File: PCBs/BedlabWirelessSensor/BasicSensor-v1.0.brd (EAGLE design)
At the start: 41.6 x 50.2 mm, 18 parts, among them U1 ATMEGA328P_PDIP

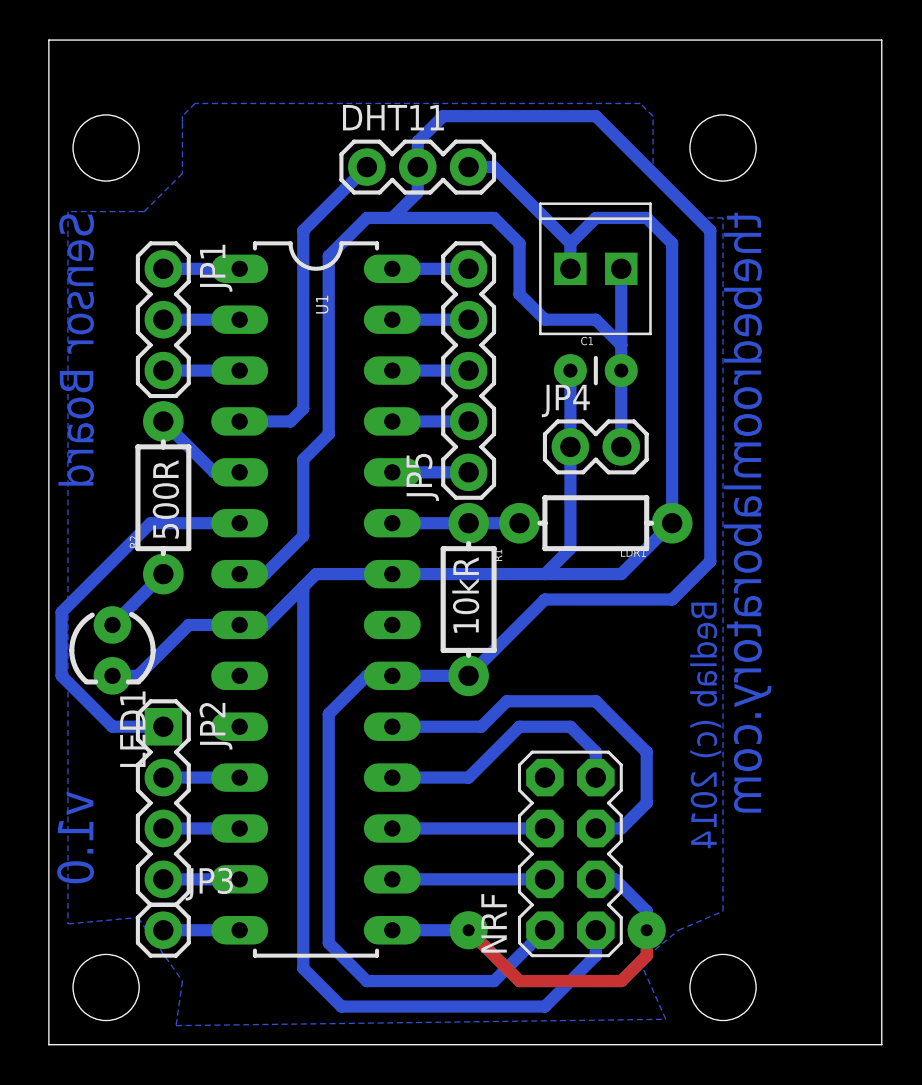
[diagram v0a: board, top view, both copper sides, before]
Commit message: Tiled PCB layout added for printing tomorrow. Additionally, changes made to arduino sketches to add funtionality for LDR, LED, Temp/humid sensor and switching the lights on/off from the gateway.
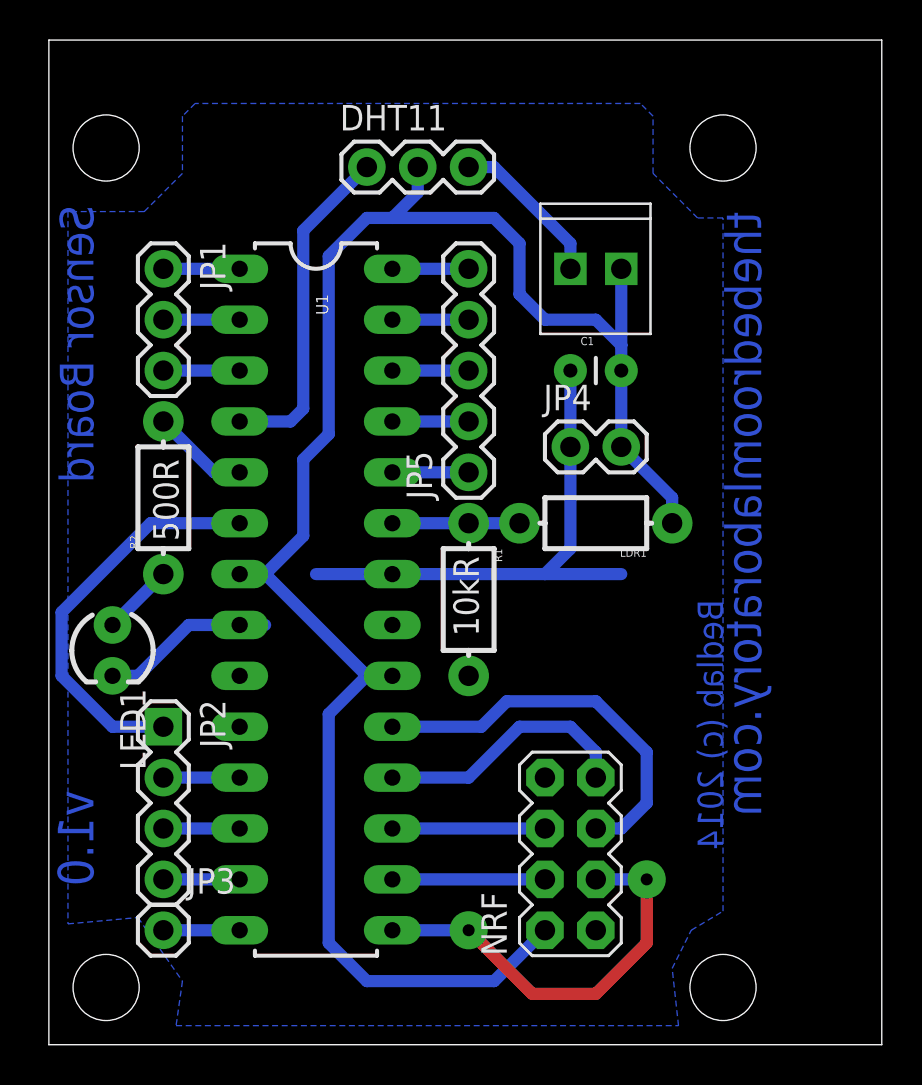
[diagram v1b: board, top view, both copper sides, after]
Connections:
- net GND: now also R1.P$2; no longer LDR1.P$1
- net VCC: now also LDR1.P$1; no longer R1.P$2
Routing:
- net GND: track 106.6 -> 42.5 mm
- net VCC: track 131.5 -> 90.0 mm
- net N$5: track 19.7 -> 20.8 mm
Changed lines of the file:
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@@
 <wire x1="0" y1="50.155" x2="0" y2="0" width="0" layer="20"/>
 <text x="35.56" y="41.5925" size="1.778" layer="16" rot="SMR270">thebedroomlaboratory.com</text>
-<text x="33.3375" y="22.225" size="1.27" layer="16" rot="SMR270">Bedlab (c) 2014</text>
-<text x="2.2225" y="41.5925" size="1.6764" layer="16" rot="SMR270">Sensor Board</text>
+<text x="33.655" y="22.225" size="1.27" layer="16" rot="SMR270">Bedlab (c) 2014</text>
+<text x="2.2225" y="41.91" size="1.6764" layer="16" rot="SMR270">Sensor Board</text>
 <text x="2.2225" y="12.7" size="1.778" layer="16" rot="SMR270">v1.0</text>
 <dimension x1="0" y1="50.155" x2="36.195" y2="47.625" x3="18.0975" y3="47.625" textsize="1.778" layer="16" dtype="horizontal"/>
@@
 </signal>
 <signal name="VCC">
-<contactref element="R1" pad="P$2"/>
 <contactref element="DHT11" pad="2"/>
 <contactref element="U1" pad="20"/>
@@
 <wire x1="13.97" y1="5.08" x2="13.97" y2="16.51" width="0.6096" layer="16"/>
 <wire x1="13.97" y1="16.51" x2="15.875" y2="18.415" width="0.6096" layer="16"/>
-<wire x1="15.875" y1="18.415" x2="17.145" y2="18.415" width="0.6096" layer="16"/>
 <wire x1="28.575" y1="33.655" x2="28.575" y2="34.925" width="0.6096" layer="16"/>
 <wire x1="28.575" y1="38.735" x2="28.575" y2="34.925" width="0.6096" layer="16"/>
@@
 <wire x1="12.7" y1="29.21" x2="13.97" y2="30.48" width="0.6096" layer="16"/>
 <wire x1="13.97" y1="30.48" x2="13.97" y2="39.37" width="0.6096" layer="16"/>
-<wire x1="20.955" y1="18.415" x2="24.765" y2="22.225" width="0.6096" layer="16"/>
-<wire x1="24.765" y1="22.225" x2="31.115" y2="22.225" width="0.6096" layer="16"/>
-<wire x1="31.115" y1="22.225" x2="33.02" y2="24.13" width="0.6096" layer="16"/>
-<wire x1="33.02" y1="24.13" x2="33.02" y2="40.64" width="0.6096" layer="16"/>
-<wire x1="33.02" y1="40.64" x2="27.305" y2="46.355" width="0.6096" layer="16"/>
-<wire x1="27.305" y1="46.355" x2="19.685" y2="46.355" width="0.6096" layer="16"/>
-<wire x1="19.685" y1="46.355" x2="18.415" y2="45.085" width="0.6096" layer="16"/>
-<wire x1="18.415" y1="45.085" x2="18.415" y2="43.815" width="0.6096" layer="16"/>
-<wire x1="17.145" y1="18.415" x2="20.955" y2="18.415" width="0.6096" layer="16"/>
+<contactref element="LDR1" pad="P$1"/>
+<wire x1="28.575" y1="29.845" x2="31.115" y2="27.305" width="0.6096" layer="16"/>
+<wire x1="31.115" y1="27.305" x2="31.115" y2="26.035" width="0.6096" layer="16"/>
+<wire x1="10.795" y1="23.495" x2="15.875" y2="18.415" width="0.6096" layer="16"/>
+<wire x1="15.875" y1="18.415" x2="17.145" y2="18.415" width="0.6096" layer="16"/>
 </signal>
 <signal name="GND">
-<contactref element="LDR1" pad="P$1"/>
 <contactref element="DHT11" pad="3"/>
 <contactref element="U1" pad="8"/>
@@
 <contactref element="C1" pad="1"/>
 <contactref element="JP4" pad="1"/>
-<wire x1="24.765" y1="1.905" x2="14.605" y2="1.905" width="0.6096" layer="16"/>
 <wire x1="3.175" y1="18.415" x2="4.445" y2="18.415" width="0.6096" layer="16"/>
 <wire x1="4.445" y1="18.415" x2="6.985" y2="20.955" width="0.6096" layer="16"/>
@@
 <wire x1="26.035" y1="24.765" x2="24.765" y2="23.495" width="0.6096" layer="16"/>
 <wire x1="24.765" y1="23.495" x2="17.145" y2="23.495" width="0.6096" layer="16"/>
-<wire x1="31.115" y1="26.035" x2="28.575" y2="23.495" width="0.6096" layer="16"/>
 <wire x1="28.575" y1="23.495" x2="24.765" y2="23.495" width="0.6096" layer="16"/>
 <wire x1="26.035" y1="38.735" x2="26.035" y2="40.005" width="0.6096" layer="16"/>
-<wire x1="26.035" y1="40.005" x2="27.305" y2="41.275" width="0.6096" layer="16"/>
-<wire x1="27.305" y1="41.275" x2="29.845" y2="41.275" width="0.6096" layer="16"/>
-<wire x1="29.845" y1="41.275" x2="31.115" y2="40.005" width="0.6096" layer="16"/>
-<wire x1="31.115" y1="40.005" x2="31.115" y2="26.035" width="0.6096" layer="16"/>
 <wire x1="26.035" y1="40.005" x2="22.225" y2="43.815" width="0.6096" layer="16"/>
 <wire x1="22.225" y1="43.815" x2="20.955" y2="43.815" width="0.6096" layer="16"/>
-<wire x1="14.605" y1="1.905" x2="12.7" y2="3.81" width="0.6096" layer="16"/>
-<wire x1="12.7" y1="3.81" x2="12.7" y2="22.86" width="0.6096" layer="16"/>
-<wire x1="12.7" y1="22.86" x2="10.795" y2="20.955" width="0.6096" layer="16"/>
 <wire x1="10.795" y1="20.955" x2="9.525" y2="20.955" width="0.6096" layer="16"/>
 <wire x1="17.145" y1="23.495" x2="13.335" y2="23.495" width="0.6096" layer="16"/>
-<wire x1="13.335" y1="23.495" x2="12.7" y2="22.86" width="0.6096" layer="16"/>
-<wire x1="27.305" y1="5.715" x2="27.305" y2="4.445" width="0.6096" layer="16"/>
-<wire x1="27.305" y1="4.445" x2="24.765" y2="1.905" width="0.6096" layer="16"/>
 <polygon width="0.4064" layer="16">
-<vertex x="6.6675" y="46.0375"/>
+<vertex x="6.6675" y="46.355"/>
 <vertex x="6.6675" y="43.4975"/>
 <vertex x="4.7625" y="41.5925"/>
@@
 <vertex x="6.6675" y="3.175"/>
 <vertex x="6.35" y="0.9525"/>
-<vertex x="30.7975" y="1.27"/>
-<vertex x="29.5275" y="4.1275"/>
-<vertex x="31.4325" y="5.715"/>
+<vertex x="31.4325" y="0.9525"/>
+<vertex x="31.115" y="3.81"/>
+<vertex x="32.0675" y="5.715"/>
 <vertex x="33.655" y="6.6675"/>
 <vertex x="33.655" y="41.275"/>
@@
 <vertex x="29.5275" y="46.99"/>
 <vertex x="7.3025" y="46.99"/>
-<vertex x="6.6675" y="46.355"/>
 </polygon>
+<contactref element="R1" pad="P$2"/>
 </signal>
 <signal name="N$2">
@@
 <wire x1="17.145" y1="5.715" x2="20.955" y2="5.715" width="0.6096" layer="16"/>
 <via x="20.955" y="5.715" extent="1-16" drill="0.6" diameter="1.905"/>
-<via x="29.845" y="5.715" extent="1-16" drill="0.6" diameter="1.905"/>
-<wire x1="20.955" y1="5.715" x2="23.495" y2="3.175" width="0.6096" layer="1"/>
-<wire x1="23.495" y1="3.175" x2="28.575" y2="3.175" width="0.6096" layer="1"/>
-<wire x1="28.575" y1="3.175" x2="29.845" y2="4.445" width="0.6096" layer="1"/>
-<wire x1="29.845" y1="4.445" x2="29.845" y2="5.715" width="0.6096" layer="1"/>
-<wire x1="27.305" y1="8.255" x2="28.2575" y2="8.255" width="0.6096" layer="16"/>
-<wire x1="28.2575" y1="8.255" x2="29.845" y2="6.6675" width="0.6096" layer="16"/>
-<wire x1="29.845" y1="6.6675" x2="29.845" y2="5.715" width="0.6096" layer="16"/>
+<via x="29.845" y="8.255" extent="1-16" drill="0.6" diameter="1.905"/>
+<wire x1="20.955" y1="5.715" x2="24.13" y2="2.54" width="0.6096" layer="1"/>
+<wire x1="24.13" y1="2.54" x2="27.305" y2="2.54" width="0.6096" layer="1"/>
+<wire x1="27.305" y1="2.54" x2="29.845" y2="5.08" width="0.6096" layer="1"/>
+<wire x1="29.845" y1="5.08" x2="29.845" y2="8.255" width="0.6096" layer="1"/>
+<wire x1="27.305" y1="8.255" x2="29.845" y2="8.255" width="0.6096" layer="16"/>
 </signal>
 <signal name="N$6">
